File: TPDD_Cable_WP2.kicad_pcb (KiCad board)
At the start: 2 copper layers, 10.6 x 12.7 mm, 5 parts, among them J1 Wire Solder Pads, J2 TPDD, Q1 DTA114EKA, Q2 DTA114EKA, Q3 DTA114EKA

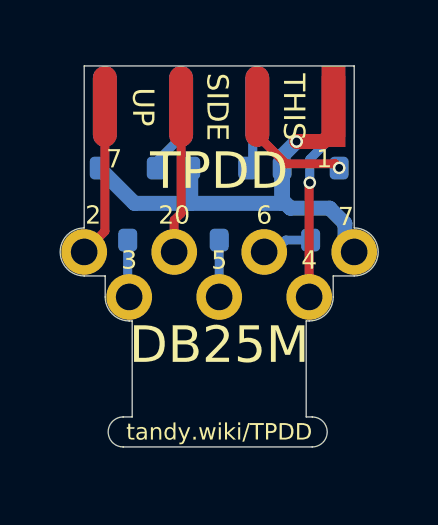
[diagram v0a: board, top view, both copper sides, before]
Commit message: add WP-2 version, add EB+ in schematics
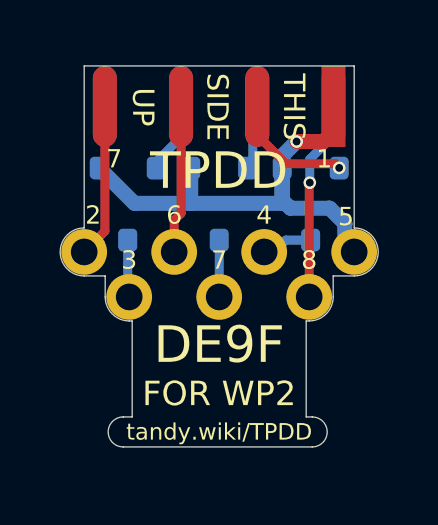
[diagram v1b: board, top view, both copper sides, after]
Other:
- board text added: "8"
- board text added: "DE9F"
- board text added: "FOR WP2"
- board text removed: "20"
- board text removed: "DB25M"
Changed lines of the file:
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@@
   (general
     (thickness 1.6)
-    (drawings 44)
+    (drawings 45)
     (tracks 48)
     (zones 0)
@@
     (36 B.SilkS user)
     (37 F.SilkS user)
-    (38 B.Mask user hide)
-    (39 F.Mask user hide)
+    (38 B.Mask user)
+    (39 F.Mask user)
     (40 Dwgs.User user hide)
     (41 Cmts.User user hide)
@@
     )
   )
+  (gr_text "FOR WP2" (at 144.993 91.8591) (layer F.SilkS)
+    (effects (font (size 0.8128 0.8128) (thickness 0.1016)))
+  )
   (gr_arc (start 148.093 93.1295) (end 148.093 93.6295) (angle -180) (layer Edge.Cuts) (width 0.0127))
   (gr_arc (start 141.793 93.1295) (end 141.793 92.6295) (angle -180) (layer Edge.Cuts) (width 0.0127))
@@
     (effects (font (size 0.6 0.6) (thickness 0.05)) (justify mirror))
   )
-  (gr_text DB25M (at 144.993 90.2295) (layer F.SilkS)
+  (gr_text DE9F (at 144.993 90.2295) (layer F.SilkS)
     (effects (font (size 1.2192 1.2192) (thickness 0.1524)))
   )
@@
     (effects (font (size 0.7112 0.7112) (thickness 0.0762)) (justify mirror))
   )
-  (gr_text 4 (at 147.993 87.4045) (layer F.SilkS)
-    (effects (font (size 0.6096 0.6096) (thickness 0.0762)))
-  )
-  (gr_text 5 (at 144.993 87.4045) (layer F.SilkS)
+  (gr_text 8 (at 147.993 87.4045) (layer F.SilkS)
+    (effects (font (size 0.6096 0.6096) (thickness 0.0762)))
+  )
+  (gr_text 7 (at 144.993 87.4045) (layer F.SilkS)
     (effects (font (size 0.6096 0.6096) (thickness 0.0762)))
   )
@@
     (effects (font (size 0.6096 0.6096) (thickness 0.0762)))
   )
-  (gr_text 20 (at 143.493 85.9045) (layer F.SilkS)
-    (effects (font (size 0.6096 0.6096) (thickness 0.0762)))
-  )
-  (gr_text 6 (at 146.493 85.9045) (layer F.SilkS)
-    (effects (font (size 0.6096 0.6096) (thickness 0.0762)))
-  )
-  (gr_text 7 (at 149.218 85.9545) (layer F.SilkS)
-    (effects (font (size 0.6096 0.6096) (thickness 0.0762)))
-  )
+  (gr_text 6 (at 143.493 85.9045) (layer F.SilkS)
+    (effects (font (size 0.6096 0.6096) (thickness 0.0762)))
+  )
+  (gr_text 4 (at 146.493 85.9045) (layer F.SilkS)
+    (effects (font (size 0.6096 0.6096) (thickness 0.0762)))
+  )
+  (gr_text 5 (at 149.218 85.9545) (layer F.SilkS)
+    (effects (font (size 0.6096 0.6096) (thickness 0.0762)))
+  )

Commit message: bigger 2x4 solder pads, smaller wire holes
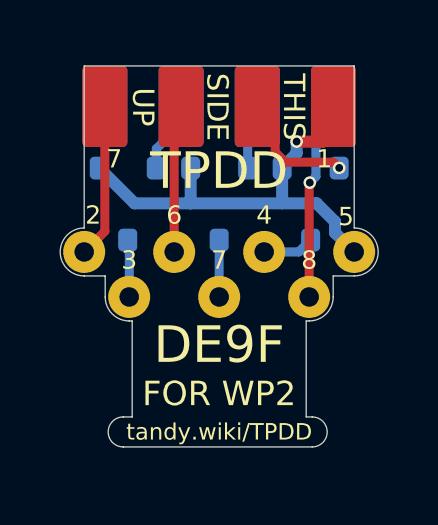
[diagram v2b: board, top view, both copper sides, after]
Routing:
- net /SG: track 16.8 -> 15.5 mm

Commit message: adjust board outline
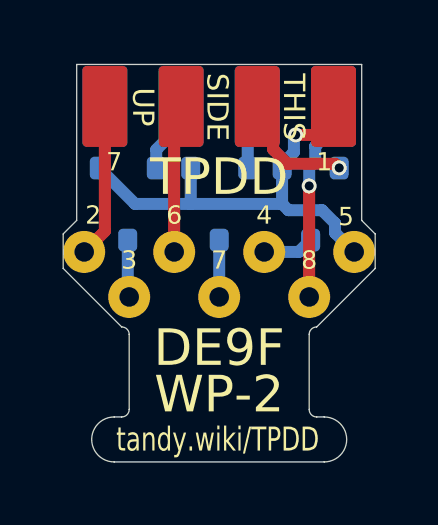
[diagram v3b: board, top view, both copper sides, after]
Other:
- board size 10.6 x 12.7 mm -> 10.4 x 13.2 mm
- net class Default: clearance 0.16 -> 0.2; trace_width 0.16 -> 0.2; via_dia 0.42 -> 0.5; via_drill 0.26 -> 0.3
- rule trace_clearance: 0.16 -> 0.2
- rule trace_min: 0.16 -> 0.2
- rule via_min_drill: 0.26 -> 0.3
- rule via_min_size: 0.42 -> 0.5
- board text added: "Q* DTA114EKA"
- board text added: "WP-2"
- board text removed: "FOR WP2"
- board text removed: "Q*: DTA114EKA"
